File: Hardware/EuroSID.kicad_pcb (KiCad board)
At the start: 2 copper layers, 213.3 x 106.6 mm, 234 parts, among them J1 GATE_2, J10 IN_2, J11 IN_3, J12 PWM_CV, J13 EXT_CON, J14 Conn_01x04_Female, J15 Eurorack Connector, J16 Conn_01x06_Male, J17 Conn_ARM_JTAG_SWD_10, J18 Power_Connector_IO, J19 Power_Connector, J2 GATE_3, J20 Digital_Connector_IO, J21 CV_Connector_IO, J22 Pot_Connector_IO, J23 Attenuverter_Connector_IO, J24 Digital_Connector, J25 CV_Connector, J26 Pot_Connector, J27 Attenuverter_Connector, J28 SID_Audio_Connector_IO, J29 SID_Audio_Connector, J3 GATE_1, J4 OUT2_CON, J5 CUTOFF_CV, J6 SHAPE_CV, J7 SET_CV, J8 OUT1_CON, J9 IN_1, Q1 MMBT3904, Q2 MMBT3904, Q3 MMBT3904, SW1 Frequency Adjust, SW10 SET_SW, SW11 FILTER_SW, SW12 FILTEREXT_SW, SW13 SHAPE_SW, SW2 MOD_SW, SW3 FILTER1_SW, SW4 PROG, SW5 VOICE_SW, SW6 FILTER2_SW, SW7 RST, SW8 MODE_SW, SW9 FILTER3_SW, U1 TLC5947DAP, U10 LM1117-3.3, U11 LM1117-5.0, U12 L7809, U13 STM32F303RBTx, U2 OPA1678, U3 MCP6004, U4 MCP6004, U6 74HC595, U7 74HC595, U8 SID, U9 LM1117-3.3, X1 ECS-8FMX-010-TR

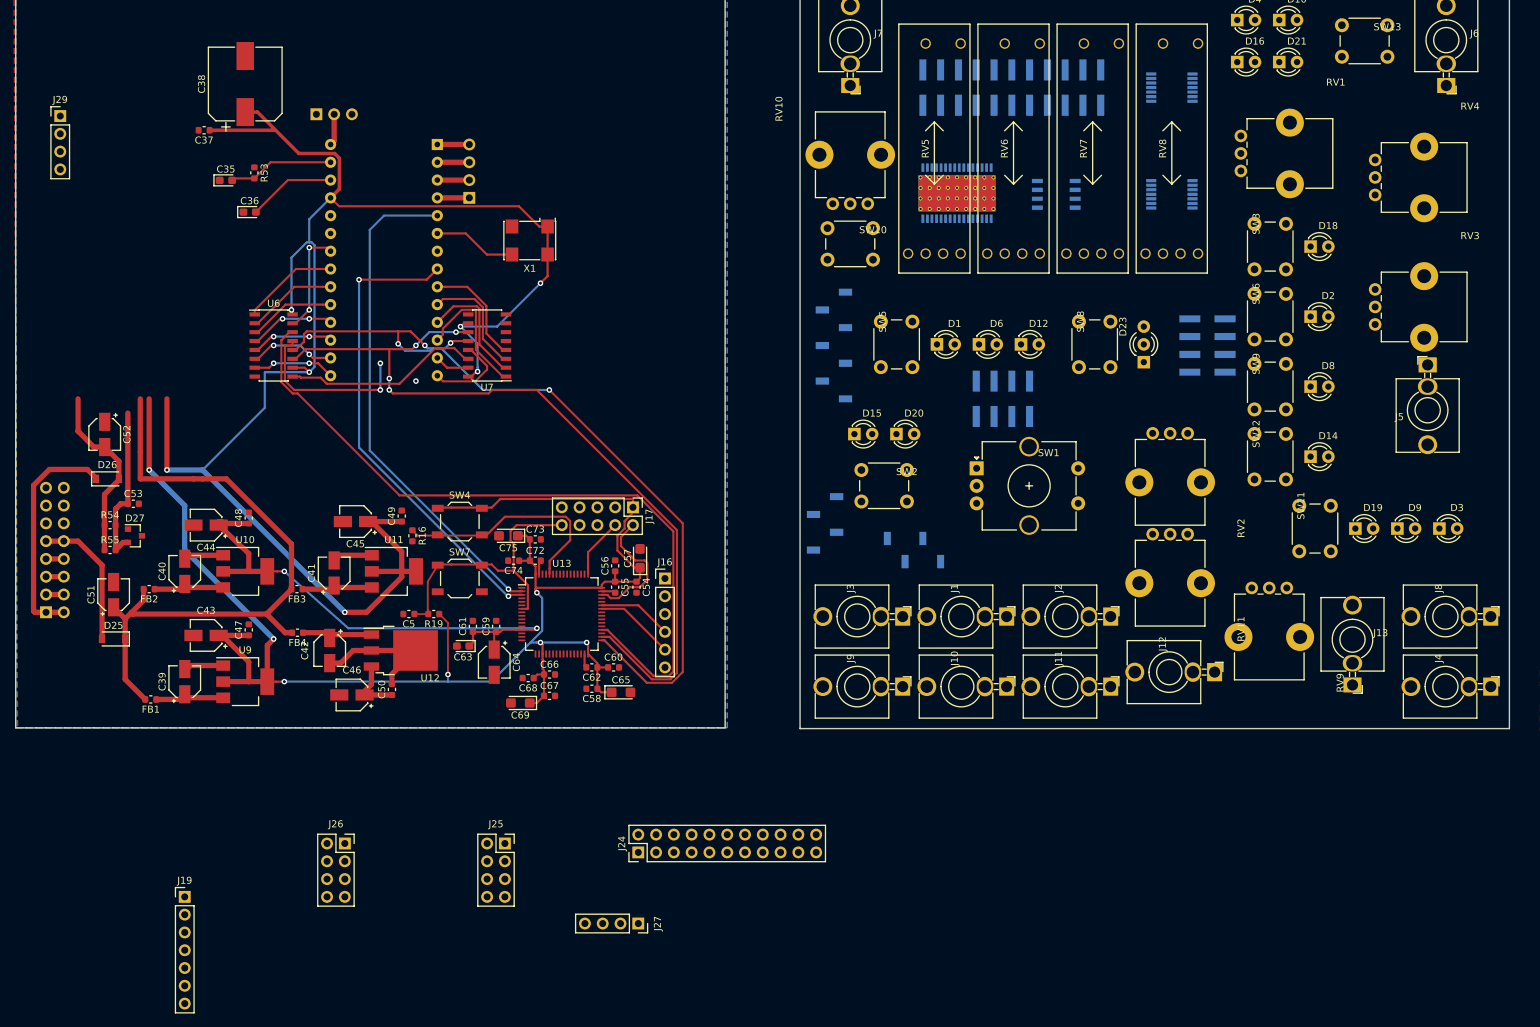
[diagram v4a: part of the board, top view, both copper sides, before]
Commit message: Fixed location of headers for board to board
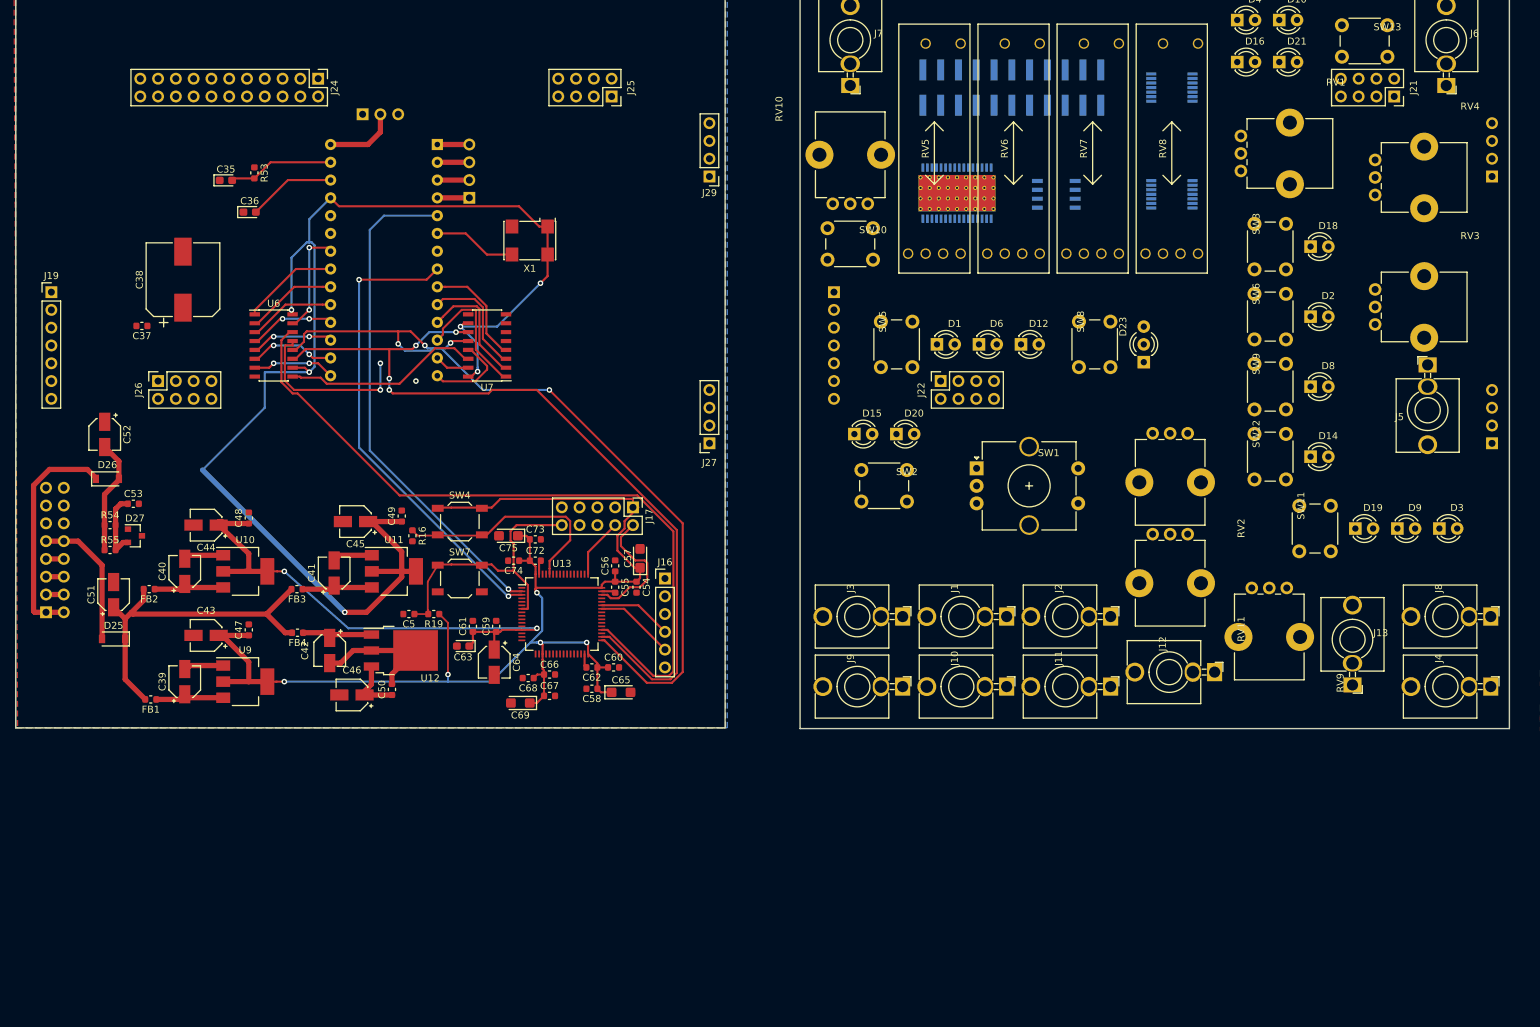
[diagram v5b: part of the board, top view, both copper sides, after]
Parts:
- J18: footprint Connector_PinSocket_2.54mm:PinSocket_1x07_P2.54mm_Vertical_SMD_Pin1Left -> Connector_PinSocket_2.54mm:PinSocket_1x07_P2.54mm_Vertical
- J21, J22: footprint Connector_PinSocket_2.54mm:PinSocket_2x04_P2.54mm_Vertical_SMD -> Connector_PinSocket_2.54mm:PinSocket_2x04_P2.54mm_Vertical; moved to F.Cu
- J23, J28: footprint Connector_PinSocket_2.54mm:PinSocket_1x04_P2.54mm_Vertical_SMD_Pin1Left -> Connector_PinSocket_2.54mm:PinSocket_1x04_P2.54mm_Vertical
- moved J24 119.6 mm to (84.4, 50.3), turned to 270 degrees
- moved J25 107.8 mm to (126.3, 52.8), turned to 270 degrees
- moved J28 107.4 mm to (252.0, 64.3)
- moved J29 93.1 mm to (140.3, 64.3), turned to 180 degrees
- moved J19 88.4 mm to (46.3, 80.8)
- moved J23 83.9 mm to (252.0, 102.4), turned to 0 degrees
- moved J26 71.2 mm to (61.5, 93.5), turned to 90 degrees
- moved J27 69.3 mm to (140.3, 102.4), turned to 180 degrees
- moved J21 44.5 mm to (238.1, 52.8), turned to 270 degrees
- moved C37 29.3 mm to (59.2, 85.6)
- moved C38 29.3 mm to (65.1, 79.0)
- moved J22 9.25 mm to (173.3, 93.5), turned to 90 degrees
- moved J18 7.62 mm to (158.0, 80.8)
- moved JP1 6.60 mm to (90.7, 55.4)
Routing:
- net +3V3: track 229.1 -> 180.9 mm, vias 7 -> 5
- net +5V: track 237.8 -> 191.0 mm, vias 7 -> 6
- net +12V: track 92.8 -> 49.5 mm
- net -10V_REF: track 23.1 -> 10.1 mm
- net -12V: track 25.8 -> 16.4 mm
- net Net-(JP1-Pad2): track 4.53 -> 10.4 mm

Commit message: Added some connector routing
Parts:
- C1, C10, C11, C12, C13, C14, C15, C16, C17, C18, C19, C2, C20, C21, C22, C23, C24, C25, C26, C27, C28, C29, C3, C30, C31, C32, C33, C34, C4, C6, C7, C70, C71, C8, C9, D24, Q1, Q2, Q3, R1, R10, R11, R12, R13, R14, R15, R17, R18, R2, R20, R21, R22, R23, R24, R25, R26, R27, R28, R29, R3, R30, R31, R32, R33, R34, R35, R36, R37, R38, R39, R4, R40, R41, R42, R43, R44, R45, R46, R47, R48, R49, R5, R50, R51, R52, R56, R6, R7, R8, R9: moved to B.Cu
- moved R29 108.4 mm to (281.9, 106.9)
- moved R33 105.9 mm to (281.9, 105.4)
- moved R35 105.9 mm to (284.9, 105.4)
- moved R36 103.6 mm to (281.9, 103.9)
- moved R41 103.6 mm to (284.9, 103.9)
- moved R37 101.2 mm to (281.9, 102.4)
- moved R42 101.2 mm to (284.9, 102.4)
- moved R40 98.9 mm to (281.9, 100.9)
- moved R43 98.9 mm to (284.9, 100.9)
- moved R44 96.6 mm to (281.9, 99.4)
- moved R4 88.7 mm to (264.0, 116.1)
- moved R21 85.8 mm to (264.0, 114.6)
- moved C1 84.6 mm to (269.3, 117.6)
- moved R13 83.0 mm to (264.0, 113.1)
- moved D24 82.9 mm to (271.1, 69.3)
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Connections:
- J20 pad 14: GATE_1_IO -> (no net)
- J20 pad 16: GATE_2_IO -> (no net)
- J20 pad 18: GATE_3_IO -> (no net)
- J24 pad 14: GATE_1 -> (no net)
- J24 pad 16: GATE_2 -> (no net)
- J24 pad 18: GATE_3 -> (no net)
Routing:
- net GATE_1: track 0.00 -> 119.3 mm, vias 0 -> 5
- net LED_CLK: track 0.00 -> 112.9 mm, vias 0 -> 6
- net +12V: track 49.5 -> 160.7 mm
- net GATE_2: track 0.00 -> 106.9 mm, vias 0 -> 5
- net LED_LATCH: track 0.00 -> 102.4 mm, vias 0 -> 2
- net GATE_3: track 0.00 -> 99.6 mm, vias 0 -> 1
- net CUTOFF: track 0.00 -> 78.4 mm, vias 0 -> 2
- net LED_DATA: track 0.00 -> 78.0 mm, vias 0 -> 3
- net ATTACK: track 0.00 -> 76.1 mm, vias 0 -> 4
- net +3.3VA: track 75.0 -> 150.3 mm
- net PWM: track 0.00 -> 75.1 mm, vias 0 -> 5
- net RESONANCE: track 0.00 -> 64.9 mm, vias 0 -> 4
- net PWM_ATTEN: track 0.00 -> 64.8 mm
- net DECAY: track 0.00 -> 64.3 mm, vias 0 -> 2
- net FREQ_ATTEN: track 0.00 -> 64.1 mm, vias 0 -> 4
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- added copper zone on F.Cu, net (none)

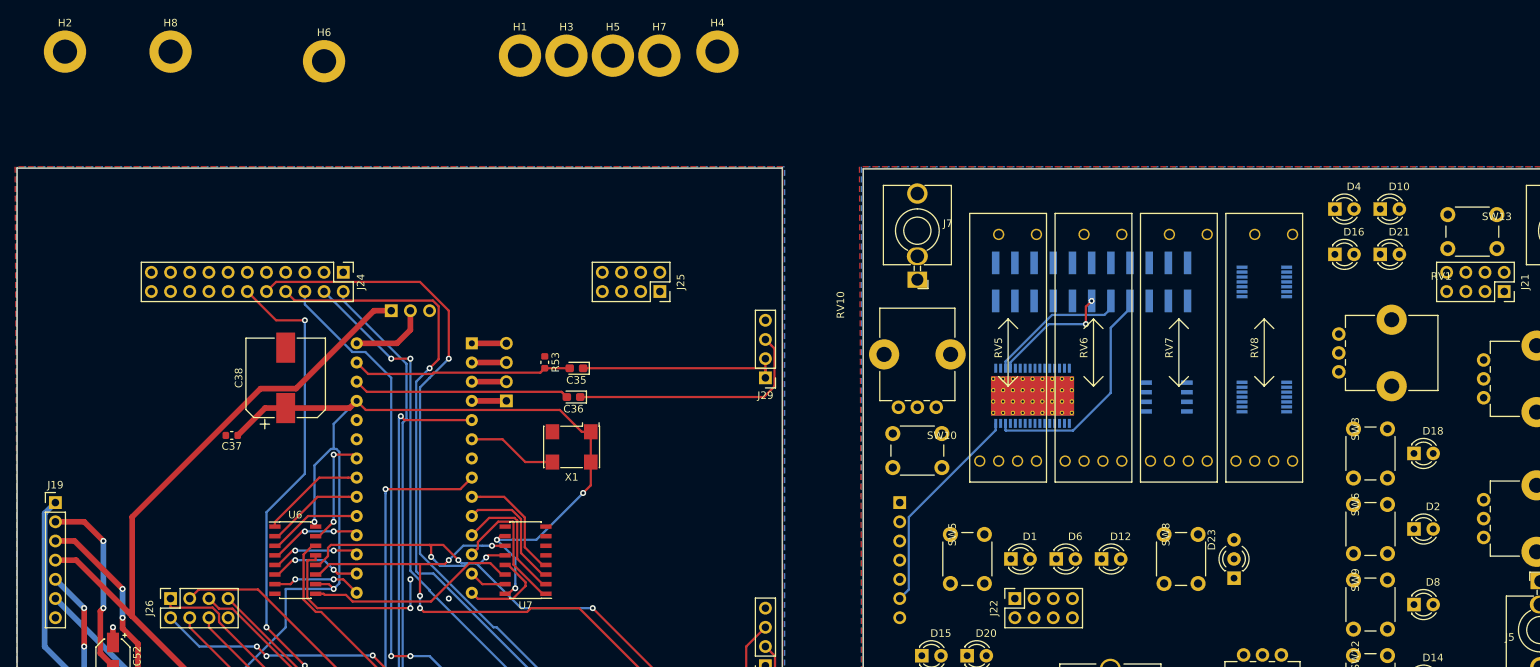
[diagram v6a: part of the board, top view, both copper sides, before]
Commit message: Corrected layout and schematic to single standoff
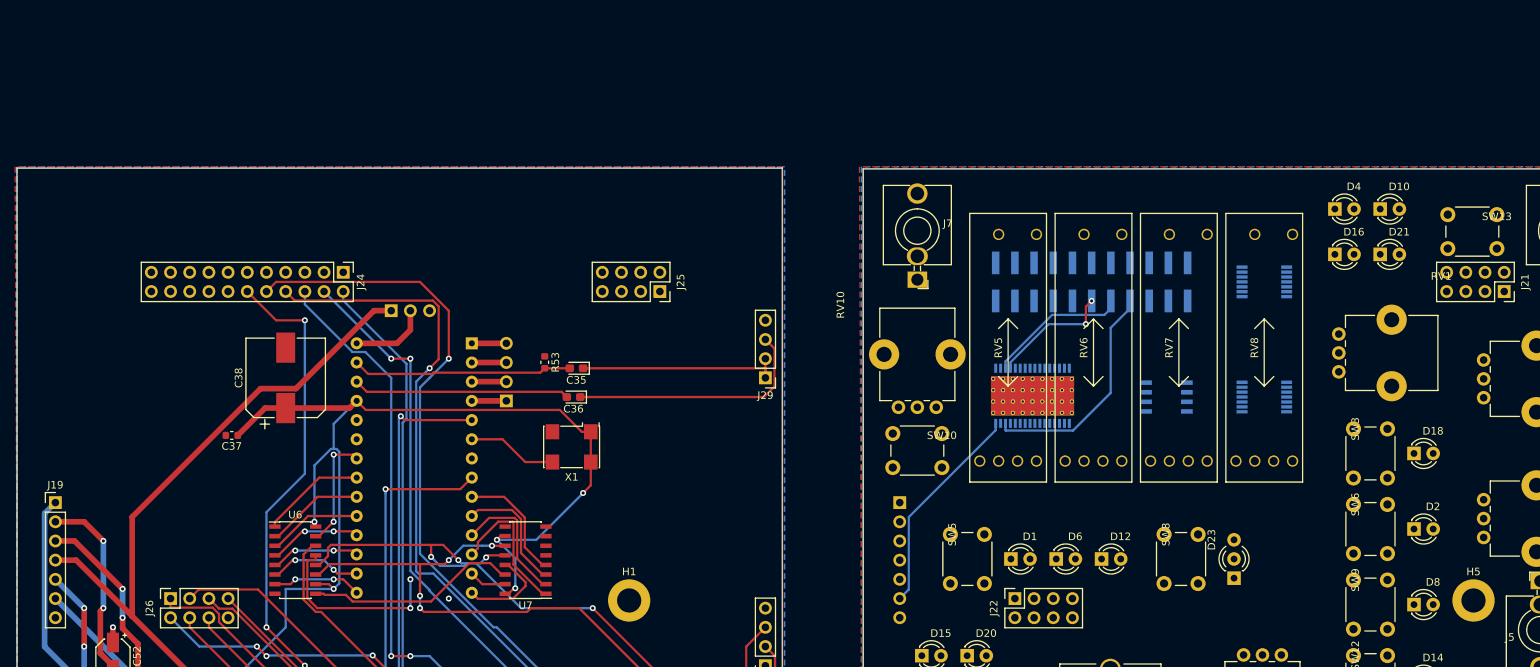
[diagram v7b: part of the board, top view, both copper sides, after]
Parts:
- removed H2, H3, H4, H6, H7, H8: MountingHole_Pad, MountingHole:MountingHole_3.2mm_M3_DIN965_Pad
- moved H5 134.8 mm to (234.0, 93.7)
- moved H1 73.5 mm to (122.2, 93.7)
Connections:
- U1 pad 10: Net-(D7-Pad1) -> (no net)
- U1 pad 11: Net-(D13-Pad1) -> (no net)
